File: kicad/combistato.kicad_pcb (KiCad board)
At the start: 2 copper layers, 119.4 x 101.6 mm, 17 parts, among them con3 4x4keypad, con4 power

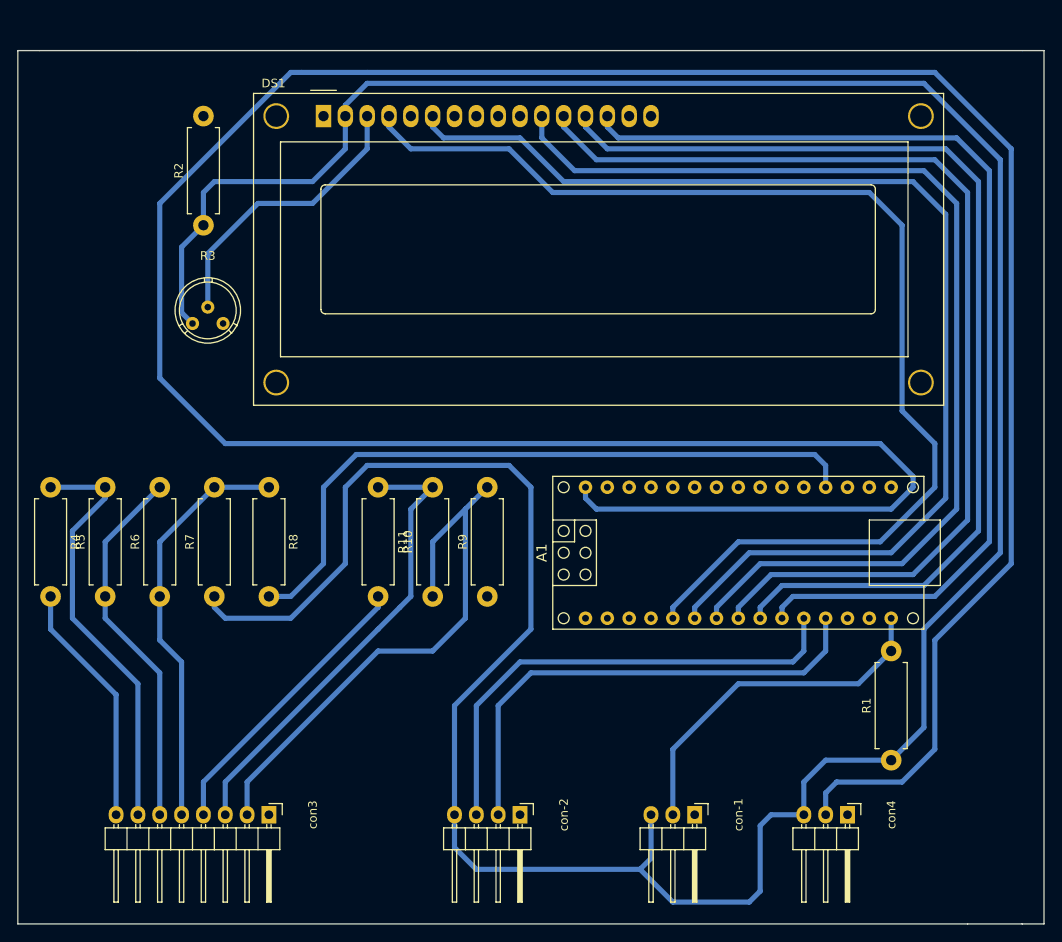
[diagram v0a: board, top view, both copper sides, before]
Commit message: trabajando en pcb, esquema de circuito y otros
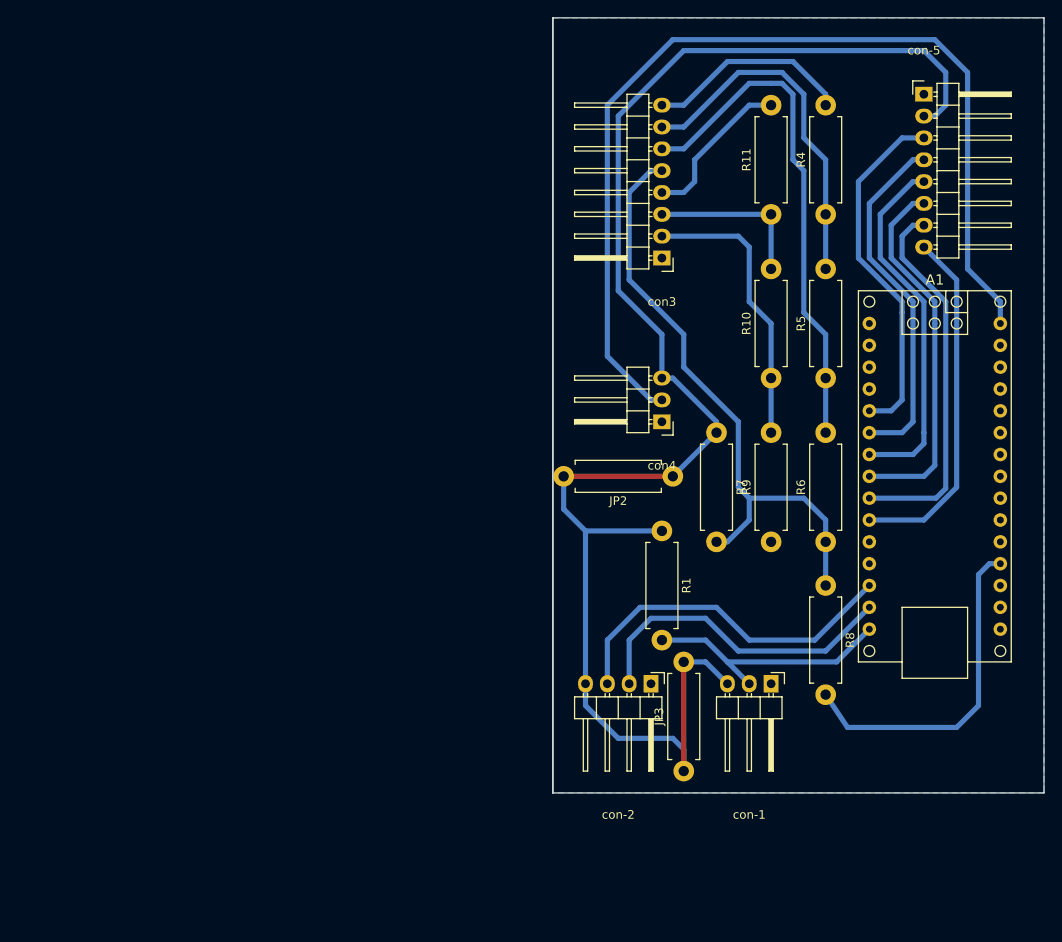
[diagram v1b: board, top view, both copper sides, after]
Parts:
- removed DS1: LCD-016N002L, LCD 1602:wc1602
- removed R2: 180, Resistores convencionales:R_Axial_DIN0411_L9.9mm_D3.6mm_P12.70mm_Horizontal
- removed R3: 10k, Potentiometers:Potentiometer_Bourns_3339H_Angular_ScrewUp
- added JP2: Jumper, Resistores convencionales:R_Axial_DIN0411_L9.9mm_D3.6mm_P12.70mm_Horizontal, F.Cu at (142.2, 72.4)
- added JP3: Jumper, Resistores convencionales:R_Axial_DIN0411_L9.9mm_D3.6mm_P12.70mm_Horizontal, F.Cu at (143.5, 106.7)
- added con-5: lcd 1602, Pin_Headers:Pin_Header_Angled_1x08, F.Cu at (171.4, 27.9)
- moved R4 95.6 mm to (160.0, 41.9), turned to 90 degrees
- moved R5 87.6 mm to (160.0, 61.0)
- moved con3 79.3 mm to (141.0, 47.0), turned to 180 degrees
- moved R6 77.7 mm to (160.0, 80.0)
- moved R8 65.8 mm to (160.0, 85.1)
- moved R7 61.4 mm to (147.3, 67.3), turned to 270 degrees
- moved R11 55.7 mm to (153.7, 41.9), turned to 90 degrees
- moved con4 50.6 mm to (141.0, 66.0), turned to 180 degrees
- moved R10 46.9 mm to (153.7, 61.0)
- moved R1 37.7 mm to (141.0, 78.7), turned to 270 degrees
- moved R9 33.6 mm to (153.7, 80.0)
- moved A1 24.5 mm to (172.7, 72.4), turned to 270 degrees
- moved con-2 21.6 mm to (139.7, 96.5)
- moved con-1 17.6 mm to (153.7, 96.5)
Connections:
- A1 pad 29: Net-(A1-Pad29) -> GND
- A1 pad 4: Net-(A1-Pad4) -> GND
- con-2 pad 2: Net-(A1-Pad12) -> Net-(A1-Pad14)
- con-2 pad 3: Net-(A1-Pad11) -> Net-(A1-Pad13)
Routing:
- net Net-(A1-Pad30): track 354.8 -> 115.1 mm
- net +5V: track 368.2 -> 182.9 mm
- net Net-(A1-Pad5): track 135.3 -> 41.6 mm
- net Net-(A1-Pad6): track 133.9 -> 41.6 mm
- net Net-(A1-Pad7): track 123.5 -> 42.3 mm
- net Net-(A1-Pad8): track 121.7 -> 43.1 mm
- net Net-(A1-Pad10): track 119.6 -> 41.3 mm
- net Net-(A1-Pad9): track 120.6 -> 43.9 mm
- net Net-(A1-Pad12): track 57.2 -> 0.00 mm
- net Net-(A1-Pad11): track 57.2 -> 0.00 mm
- net Net-(A1-Pad13): track 0.00 -> 41.3 mm
- net Net-(A1-Pad19): track 79.9 -> 39.2 mm
- net Net-(A1-Pad14): track 0.00 -> 37.8 mm
- net Net-(R10-Pad2): track 54.4 -> 19.0 mm
- net Net-(DS1-Pad3): track 33.6 -> 0.00 mm
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- added copper zone on B.Cu, net GND
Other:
- board size 119.4 x 101.6 mm -> 57.1 x 90.2 mm
